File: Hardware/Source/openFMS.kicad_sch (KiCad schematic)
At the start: 36 parts, among them U1 STM32F030F4Px, U4 ITR9608-F

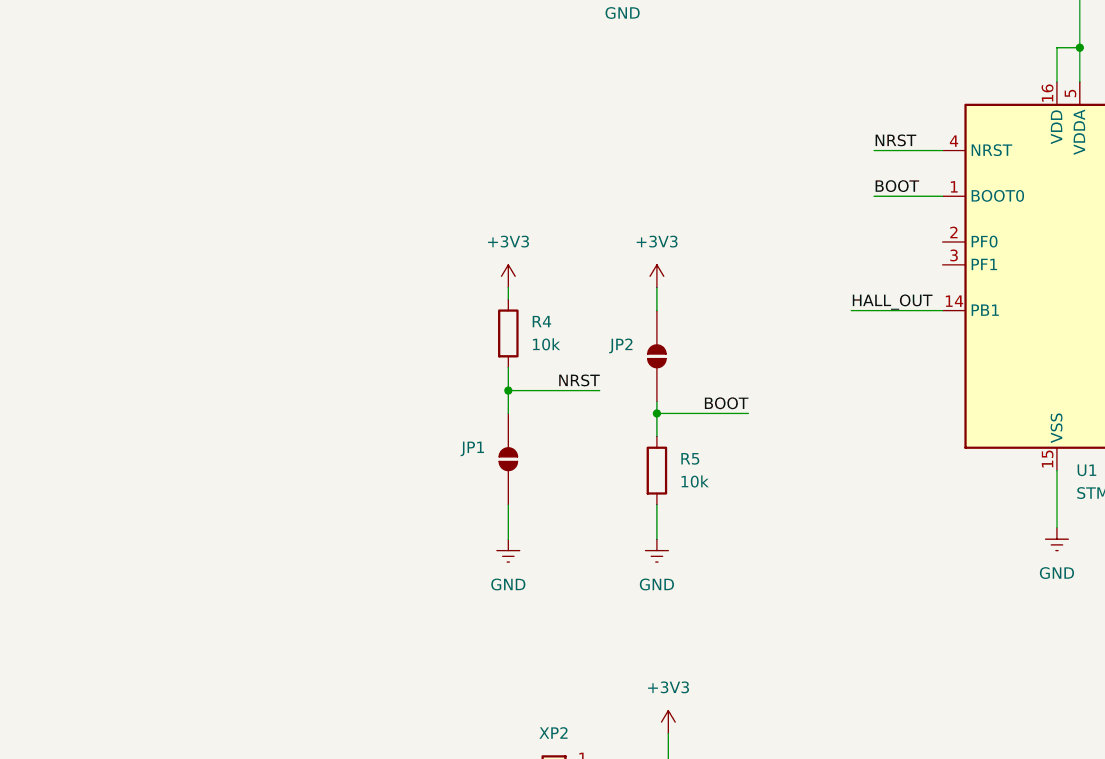
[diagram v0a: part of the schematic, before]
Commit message: Add Quartz Resonator to sheme
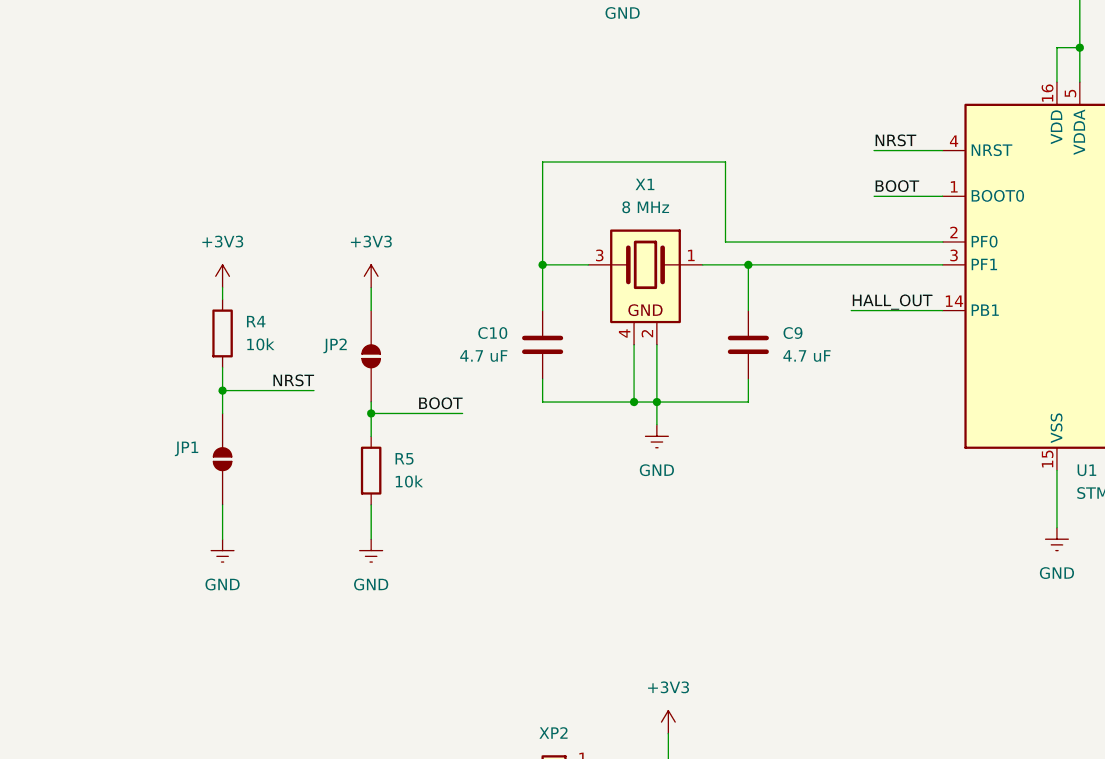
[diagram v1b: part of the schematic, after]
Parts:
- added C10, C9: 4.7 uF, Capacitor_SMD:C_0603_1608Metric, symbol Device:C
- added X1: 8 MHz, Crystal_AKL:Crystal_SMD_5032-4Pin_5.0x3.2mm, symbol Crystal_AKL:SMD5032-4
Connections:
- net GND: now also C10.2, C9.2, X1.2, X1.4
- net at U1.2 (PF0): now also C10.1, X1.3
- net at U1.3 (PF1): now also C9.1, X1.1
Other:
- moved on the sheet: JP1, JP2, R4, R5
